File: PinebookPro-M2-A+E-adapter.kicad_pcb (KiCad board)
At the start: 2 copper layers, 70.5 x 32 mm, 30 parts, among them J1 Conn_01x35_MountingPin, J2 M.2-NGFF-A+E-Key, U1 TPS63001

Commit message: Add GND testpoints
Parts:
- added TP10: TestPoint, TestPoint:TestPoint_Pad_2.0x2.0mm, F.Cu at (163.5, 102.0)
- added TP9: TestPoint, TestPoint:TestPoint_Pad_2.0x2.0mm, F.Cu at (181.5, 102.0)
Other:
- board text added: "GND"
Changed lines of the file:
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@@
   (general
     (thickness 1)
-    (drawings 22)
+    (drawings 24)
     (tracks 503)
     (zones 0)
-    (modules 30)
+    (modules 32)
     (nets 68)
   )
@@
     (add_net "Net-(L1-Pad2)")
     (add_net "Net-(R1-Pad2)")
+  )
+  (module TestPoint:TestPoint_Pad_2.0x2.0mm (layer F.Cu)
+    (at 163.5 102)
+    (descr "SMD rectangular pad as test Point, square 2.0mm side length")
+    (tags "test point SMD pad rectangle square")
+    (attr virtual)
+    (fp_text reference TP10 (at 0 -1.998) (layer F.SilkS) hide
+      (effects (font (size 1 1) (thickness 0.15)))
+    )
+    (fp_text value TestPoint (at 0 2.05) (layer F.Fab)
+      (effects (font (size 1 1) (thickness 0.15)))
+    )
+    (fp_line (start 1.5 1.5) (end -1.5 1.5) (layer F.CrtYd) (width 0.05))
+    (fp_line (start 1.5 1.5) (end 1.5 -1.5) (layer F.CrtYd) (width 0.05))
+    (fp_line (start -1.5 -1.5) (end -1.5 1.5) (layer F.CrtYd) (width 0.05))
+    (fp_line (start -1.5 -1.5) (end 1.5 -1.5) (layer F.CrtYd) (width 0.05))
+    (fp_line (start -1.2 1.2) (end -1.2 -1.2) (layer F.SilkS) (width 0.12))
+    (fp_line (start 1.2 1.2) (end -1.2 1.2) (layer F.SilkS) (width 0.12))
+    (fp_line (start 1.2 -1.2) (end 1.2 1.2) (layer F.SilkS) (width 0.12))
+    (fp_line (start -1.2 -1.2) (end 1.2 -1.2) (layer F.SilkS) (width 0.12))
+    (fp_text user %R (at 0 -2) (layer F.Fab)
+      (effects (font (size 1 1) (thickness 0.15)))
+    )
+    (pad 1 smd rect (at 0 0) (size 2 2) (layers F.Cu F.Mask)
+      (net 1 GND))
+  )
+  (module TestPoint:TestPoint_Pad_2.0x2.0mm (layer F.Cu)
+    (at 181.5 102)
+    (descr "SMD rectangular pad as test Point, square 2.0mm side length")
+    (tags "test point SMD pad rectangle square")
+    (attr virtual)
+    (fp_text reference TP9 (at 0 -1.998) (layer F.SilkS) hide
+      (effects (font (size 1 1) (thickness 0.15)))
+    )
+    (fp_text value TestPoint (at 0 2.05) (layer F.Fab)
+      (effects (font (size 1 1) (thickness 0.15)))
+    )
+    (fp_line (start 1.5 1.5) (end -1.5 1.5) (layer F.CrtYd) (width 0.05))
+    (fp_line (start 1.5 1.5) (end 1.5 -1.5) (layer F.CrtYd) (width 0.05))
+    (fp_line (start -1.5 -1.5) (end -1.5 1.5) (layer F.CrtYd) (width 0.05))
+    (fp_line (start -1.5 -1.5) (end 1.5 -1.5) (layer F.CrtYd) (width 0.05))
+    (fp_line (start -1.2 1.2) (end -1.2 -1.2) (layer F.SilkS) (width 0.12))
+    (fp_line (start 1.2 1.2) (end -1.2 1.2) (layer F.SilkS) (width 0.12))
+    (fp_line (start 1.2 -1.2) (end 1.2 1.2) (layer F.SilkS) (width 0.12))
+    (fp_line (start -1.2 -1.2) (end 1.2 -1.2) (layer F.SilkS) (width 0.12))
+    (fp_text user %R (at 0 -2) (layer F.Fab)
+      (effects (font (size 1 1) (thickness 0.15)))
+    )
+    (pad 1 smd rect (at 0 0) (size 2 2) (layers F.Cu F.Mask)
+      (net 1 GND))
   )
   (module PinebookPro-M2-A+E-adapter:awaiting (layer B.Cu)
@@
     )
   )
+  (gr_text GND (at 163.5 104) (layer F.SilkS)
+    (effects (font (size 1 1) (thickness 0.15)))
+  )
+  (gr_text GND (at 181.5 105 270) (layer F.SilkS)
+    (effects (font (size 1 1) (thickness 0.15)))
+  )
   (gr_text JLCJLCJLCJLC (at 160.6 115.5 90) (layer F.SilkS)
     (effects (font (size 1 1) (thickness 0.15)))
@@
     (effects (font (size 1 1) (thickness 0.15)) (justify left))
   )
-  (gr_text +3V3 (at 163 102) (layer F.SilkS)
+  (gr_text +3V3 (at 159 104) (layer F.SilkS)
     (effects (font (size 1 1) (thickness 0.15)))
   )

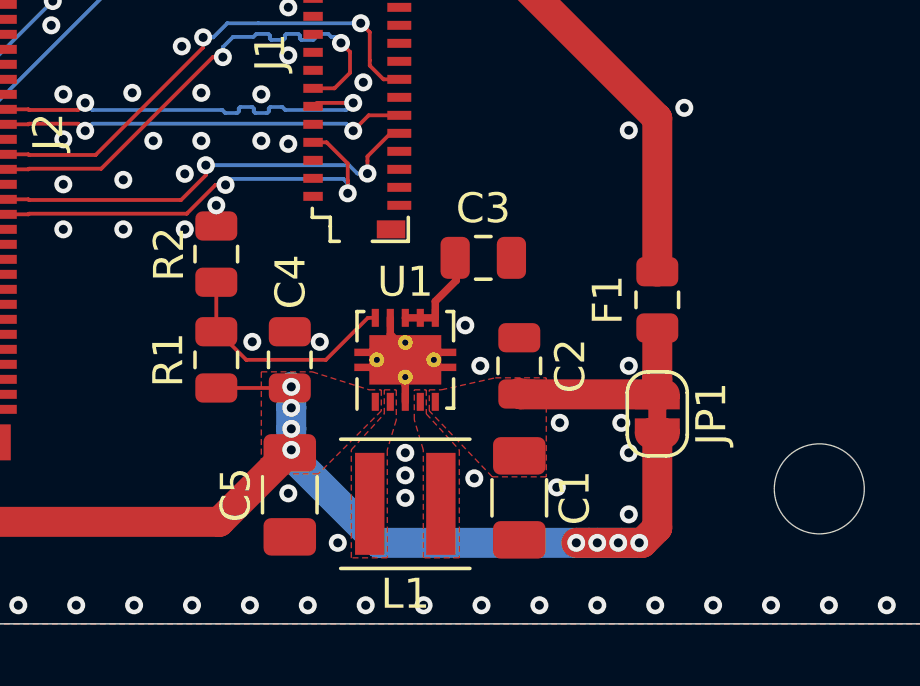
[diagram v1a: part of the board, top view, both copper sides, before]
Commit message: Add VINA strapping resistor
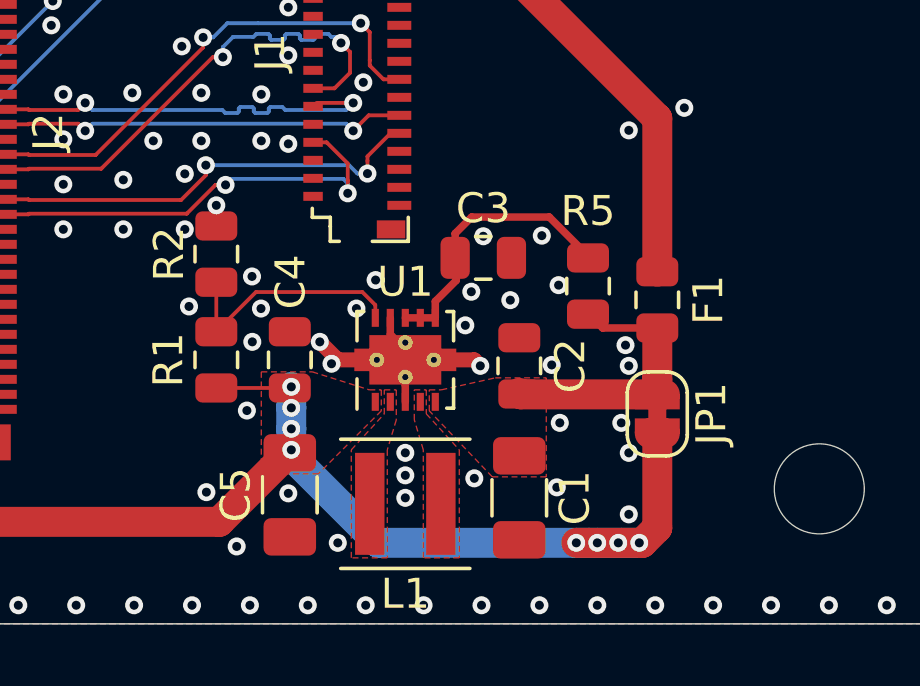
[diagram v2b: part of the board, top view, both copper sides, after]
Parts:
- added R5: 100 R, Resistor_SMD:R_0805_2012Metric, F.Cu at (184.0, 120.7)
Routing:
- net Net-(C3-Pad1): track 3.29 -> 9.32 mm
- net GND: track 3.01 -> 7.74 mm, vias 209 -> 225
- net Net-(C1-Pad1): track 6.77 -> 9.28 mm
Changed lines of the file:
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@@
     (thickness 1)
     (drawings 24)
-    (tracks 503)
+    (tracks 530)
     (zones 0)
-    (modules 32)
+    (modules 33)
     (nets 68)
   )
@@
   )
   (setup
-    (last_trace_width 0.127)
+    (last_trace_width 0.5)
     (user_trace_width 0.127)
     (user_trace_width 0.25)
@@
     (pcbplotparams
       (layerselection 0x010fc_ffffffff)
-      (usegerberextensions false)
+      (usegerberextensions true)
       (usegerberattributes false)
       (usegerberadvancedattributes false)
@@
       (outputformat 1)
       (mirror false)
-      (drillshape 1)
+      (drillshape 0)
       (scaleselection 1)
-      (outputdirectory ""))
+      (outputdirectory "fab/"))
   )
   (net 0 "")
@@
     (add_net "Net-(L1-Pad2)")
     (add_net "Net-(R1-Pad2)")
+  )
+  (module Resistor_SMD:R_0805_2012Metric (layer F.Cu)
+    (at 183.99 120.74 90)
+    (descr "Resistor SMD 0805 (2012 Metric), square (rectangular) end terminal, IPC_7351 nominal, (Body size source: https://docs.google.com/spreadsheets/d/1BsfQQcO9C6DZCsRaXUlFlo91Tg2WpOkGARC1WS5S8t0/edit?usp=sharing), generated with kicad-footprint-generator")
+    (tags resistor)
+    (attr smd)
+    (fp_text reference R5 (at 2.5 0 180) (layer F.SilkS)
+      (effects (font (size 1 1) (thickness 0.15)))
+    )
+    (fp_text value "100 R" (at 0 1.65 90) (layer F.Fab)
+      (effects (font (size 1 1) (thickness 0.15)))
+    )
+    (fp_text user %R (at 0 0 90) (layer F.Fab)
+      (effects (font (size 0.5 0.5) (thickness 0.08)))
+    )
+    (fp_line (start 1.68 0.95) (end -1.68 0.95) (layer F.CrtYd) (width 0.05))
+    (fp_line (start 1.68 -0.95) (end 1.68 0.95) (layer F.CrtYd) (width 0.05))
+    (fp_line (start -1.68 -0.95) (end 1.68 -0.95) (layer F.CrtYd) (width 0.05))
+    (fp_line (start -1.68 0.95) (end -1.68 -0.95) (layer F.CrtYd) (width 0.05))
+    (fp_line (start -0.258578 0.71) (end 0.258578 0.71) (layer F.SilkS) (width 0.12))
+    (fp_line (start -0.258578 -0.71) (end 0.258578 -0.71) (layer F.SilkS) (width 0.12))
+    (fp_line (start 1 0.6) (end -1 0.6) (layer F.Fab) (width 0.1))
+    (fp_line (start 1 -0.6) (end 1 0.6) (layer F.Fab) (width 0.1))
+    (fp_line (start -1 -0.6) (end 1 -0.6) (layer F.Fab) (width 0.1))
+    (fp_line (start -1 0.6) (end -1 -0.6) (layer F.Fab) (width 0.1))
+    (pad 2 smd roundrect (at 0.9375 0 90) (size 0.975 1.4) (layers F.Cu F.Paste F.Mask) (roundrect_rratio 0.25)
+      (net 3 "Net-(C3-Pad1)"))
+    (pad 1 smd roundrect (at -0.9375 0 90) (size 0.975 1.4) (layers F.Cu F.Paste F.Mask) (roundrect_rratio 0.25)
+      (net 2 "Net-(C1-Pad1)"))
+    (model ${KISYS3DMOD}/Resistor_SMD.3dshapes/R_0805_2012Metric.wrl
+      (at (xyz 0 0 0))
+      (scale (xyz 1 1 1))
+      (rotate (xyz 0 0 0))
+    )
   )
   (module TestPoint:TestPoint_Pad_2.0x2.0mm (layer F.Cu)
@@
     (tags resistor)
     (attr smd)
-    (fp_text reference F1 (at 0 -1.65 90) (layer F.SilkS)
+    (fp_text reference F1 (at 0 1.7 90) (layer F.SilkS)
       (effects (font (size 1 1) (thickness 0.15)))
     )
@@
   (via (at 128.55 108.4) (size 0.6) (drill 0.3) (layers F.Cu B.Cu) (net 1))
   (via (at 128.55 123.1) (size 0.6) (drill 0.3) (layers F.Cu B.Cu) (net 1))
+  (via (at 180.5 119.08) (size 0.6) (drill 0.3) (layers F.Cu B.Cu) (net 1))
+  (via (at 182.45 119.06) (size 0.6) (drill 0.3) (layers F.Cu B.Cu) (net 1))
+  (via (at 183.01 120.71) (size 0.6) (drill 0.3) (layers F.Cu B.Cu) (net 1))
+  (via (at 185.24 122.71) (size 0.6) (drill 0.3) (layers F.Cu B.Cu) (net 1))
+  (segment (start 180.2 123.2) (end 180.4 123.4) (width 0.5) (layer F.Cu) (net 1))
+  (segment (start 177.9 123.2) (end 180.2 123.2) (width 0.5) (layer F.Cu) (net 1))
+  (segment (start 175.65 123.2) (end 175.59 123.14) (width 0.5) (layer F.Cu) (net 1))
+  (segment (start 176.95 123.2) (end 175.65 123.2) (width 0.5) (layer F.Cu) (net 1))
+  (via (at 176.27 121.49) (size 0.6) (drill 0.3) (layers F.Cu B.Cu) (net 1))
+  (via (at 173.09 121.49) (size 0.6) (drill 0.3) (layers F.Cu B.Cu) (net 1))
+  (via (at 172.79 120.42) (size 0.6) (drill 0.3) (layers F.Cu B.Cu) (net 1))
+  (via (at 176.91 120.54) (size 0.6) (drill 0.3) (layers F.Cu B.Cu) (net 1))
+  (segment (start 175.59 123.14) (end 175.05 122.6) (width 0.5) (layer F.Cu) (net 1))
+  (via (at 175.44 123.33) (size 0.6) (drill 0.3) (layers F.Cu B.Cu) (net 1))
+  (via (at 182.78 123.37) (size 0.6) (drill 0.3) (layers F.Cu B.Cu) (net 1))
+  (via (at 181.4 121.21) (size 0.6) (drill 0.3) (layers F.Cu B.Cu) (net 1))
+  (via (at 180.1 120.93) (size 0.6) (drill 0.3) (layers F.Cu B.Cu) (net 1))
+  (via (at 170.69 121.42) (size 0.6) (drill 0.3) (layers F.Cu B.Cu) (net 1))
+  (via (at 172.62 124.89) (size 0.6) (drill 0.3) (layers F.Cu B.Cu) (net 1))
+  (via (at 171.27 127.61) (size 0.6) (drill 0.3) (layers F.Cu B.Cu) (net 1))
+  (via (at 172.28 129.42) (size 0.6) (drill 0.3) (layers F.Cu B.Cu) (net 1))
   (segment (start 186.3 124.35) (end 181.75 124.35) (width 1) (layer F.Cu) (net 2))
   (segment (start 181.75 124.35) (end 181.7 124.3) (width 1) (layer F.Cu) (net 2))
   (segment (start 186.3 124.35) (end 186.3 123.85) (width 1) (layer F.Cu) (net 2))
   (segment (start 186.3 123.85) (end 186.3 122.2) (width 1) (layer F.Cu) (net 2))
+  (segment (start 186.3 122.1375) (end 184.4775 122.1375) (width 0.25) (layer F.Cu) (net 2))
+  (segment (start 184.4775 122.1375) (end 183.99 121.65) (width 0.25) (layer F.Cu) (net 2))
   (segment (start 177.9 121.8) (end 178.9 121.8) (width 0.25) (layer F.Cu) (net 3))
   (segment (start 178.9 121.25) (end 179.6 120.55) (width 0.25) (layer F.Cu) (net 3))
   (segment (start 178.9 121.8) (end 178.9 121.25) (width 0.25) (layer F.Cu) (net 3))
   (segment (start 179.6 120.55) (end 179.6 119.8) (width 0.25) (layer F.Cu) (net 3))
+  (segment (start 179.5625 119.8) (end 179.5625 118.9875) (width 0.25) (layer F.Cu) (net 3))
+  (segment (start 179.5625 118.9875) (end 180.11 118.44) (width 0.25) (layer F.Cu) (net 3))
+  (segment (start 180.11 118.44) (end 182.7 118.44) (width 0.25) (layer F.Cu) (net 3))
+  (segment (start 182.7 118.44) (end 184.01 119.75) (width 0.25) (layer F.Cu) (net 3))
   (segment (start 186.3 125.65) (end 186.3 128.8) (width 1) (layer F.Cu) (net 4))
   (via (at 183.6 129.3) (size 0.6) (drill 0.3) (layers F.Cu B.Cu) (net 4))
@@
   (segment (start 167.328737 105.799415) (end 167.112409 106.015744) (width 0.127) (layer F.Cu) (net 50))
   (segment (start 166.906574 105.947133) (end 166.906571 105.947133) (width 0.127) (layer F.Cu) (net 50))
-  (segment (start 176.653 121.8) (end 175.253 123.2) (width 0.127) (layer F.Cu) (net 53))
-  (segment (start 176.9 121.8) (end 176.653 121.8) (width 0.127) (layer F.Cu) (net 53))
-  (segment (start 175.253 123.2) (end 172.6 123.2) (width 0.127) (layer F.Cu) (net 53))
-  (segment (start 172.6 123.2) (end 171.6 122.2) (width 0.127) (layer F.Cu) (net 53))
   (segment (start 171.6 122.2625) (end 171.6 120.6) (width 0.127) (layer F.Cu) (net 53))
+  (segment (start 171.6 122.2625) (end 172.9225 120.94) (width 0.127) (layer F.Cu) (net 53))
+  (segment (start 176.467 120.94) (end 176.9 121.373) (width 0.127) (layer F.Cu) (net 53))
+  (segment (start 172.9225 120.94) (end 176.467 120.94) (width 0.127) (layer F.Cu) (net 53))
+  (segment (start 176.9 121.373) (end 176.9 121.8) (width 0.127) (layer F.Cu) (net 53))
   (zone (net 1) (net_name GND) (layer F.Cu) (hatch edge 0.508)
     (connect_pads yes (clearance 0.127))

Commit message: Rev A
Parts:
- added G***: LOGO, PinebookPro-M2-A+E-adapter:manjaro, F.Cu at (191.5, 116.0)
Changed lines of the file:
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@@
     (tracks 530)
     (zones 0)
-    (modules 33)
+    (modules 34)
     (nets 68)
   )
@@
     (add_net "Net-(L1-Pad2)")
     (add_net "Net-(R1-Pad2)")
+  )
+  (module PinebookPro-M2-A+E-adapter:manjaro (layer F.Cu)
+    (at 191.5 116)
+    (fp_text reference G*** (at 0 0) (layer F.SilkS) hide
+      (effects (font (size 1.524 1.524) (thickness 0.3)))
+    )
+    (fp_text value LOGO (at 0.75 0) (layer F.SilkS) hide
+      (effects (font (size 1.524 1.524) (thickness 0.3)))
+    )
+    (fp_poly (pts (xy 3.824941 3.824941) (xy 1.673411 3.824941) (xy 1.673411 -3.824941) (xy 3.824941 -3.824941)
+      (xy 3.824941 3.824941)) (layer F.SilkS) (width 0.01))
+    (fp_poly (pts (xy 1.075764 3.824941) (xy -1.075765 3.824941) (xy -1.075765 -1.075765) (xy 1.075764 -1.075765)
+      (xy 1.075764 3.824941)) (layer F.SilkS) (width 0.01))
+    (fp_poly (pts (xy 1.075764 -1.673412) (xy -1.673412 -1.673412) (xy -1.673412 3.824941) (xy -3.824941 3.824941)
+      (xy -3.824941 -3.824941) (xy 1.075764 -3.824941) (xy 1.075764 -1.673412)) (layer F.SilkS) (width 0.01))
   )
   (module Resistor_SMD:R_0805_2012Metric (layer F.Cu)
@@
       (rotate (xyz 0 0 0))
     )
+    (model ${KIPRJMOD}/lib/DRC0010J.stp
+      (at (xyz 0 0 0))
+      (scale (xyz 1 1 1))
+      (rotate (xyz 0 0 0))
+    )
   )
   (module MountingHole:MountingHole_2.2mm_M2_Pad_Via (layer F.Cu)
@@
   (module Connector_FFC_Hirose:Hirose_FH26-35S-0.3SH_2x35-1MP_P0.30mm_Horizontal (layer F.Cu)
     (at 176.3 112.95 90)
+    (attr smd)
     (fp_text reference J1 (at 0 -2.9 90) (layer F.SilkS)
       (effects (font (size 1 1) (thickness 0.15)))
@@
     (pad 1 smd rect (at -5.1 1.4 90) (size 0.3 0.8) (layers F.Cu F.Paste F.Mask)
       (net 1 GND))
+    (model ${KIPRJMOD}/lib/ayf333535-closed.step
+      (at (xyz 0 0 0))
+      (scale (xyz 1 1 1))
+      (rotate (xyz -90 0 0))
+    )
   )
   (module MountingHole:MountingHole_3mm (layer F.Cu)
@@
       (scale (xyz 1 1 1))
       (rotate (xyz 0 0 0))
+    )
+    (model ${KIPRJMOD}/lib/Coilcraft-XAL4020.step
+      (at (xyz 0 0 0))
+      (scale (xyz 1 1 1))
+      (rotate (xyz -90 0 0))
     )
   )
@@
     (pad "" np_thru_hole circle (at -10 0 270) (size 1.1 1.1) (drill 1.1) (layers *.Cu *.Mask))
     (pad "" np_thru_hole circle (at 10 0 270) (size 1.6 1.6) (drill 1.6) (layers *.Cu *.Mask))
+    (model ${KIPRJMOD}/lib/c-2199230-3-b2-3d.stp
+      (offset (xyz 0 -2.5 2))
+      (scale (xyz 1 1 1))
+      (rotate (xyz -90 0 0))
+    )
+    (model ${KIPRJMOD}/lib/wifi-card-model.step
+      (offset (xyz 0 2 2.5))
+      (scale (xyz 1 1 1))
+      (rotate (xyz 0 0 -180))
+    )
   )
   (module Fuse:Fuse_0805_2012Metric (layer F.Cu)
